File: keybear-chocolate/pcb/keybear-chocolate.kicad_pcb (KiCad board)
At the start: 2 copper layers, 136.9 x 98.2 mm, 102 parts, among them J1 MJ-4PP-9, J2 BATT, J3 LED, J4 OLED, SW1 SW_PUSH, SW10 SW_PUSH, SW11 SW_PUSH, SW12 SW_PUSH, SW13 SW_PUSH, SW14 SW_PUSH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

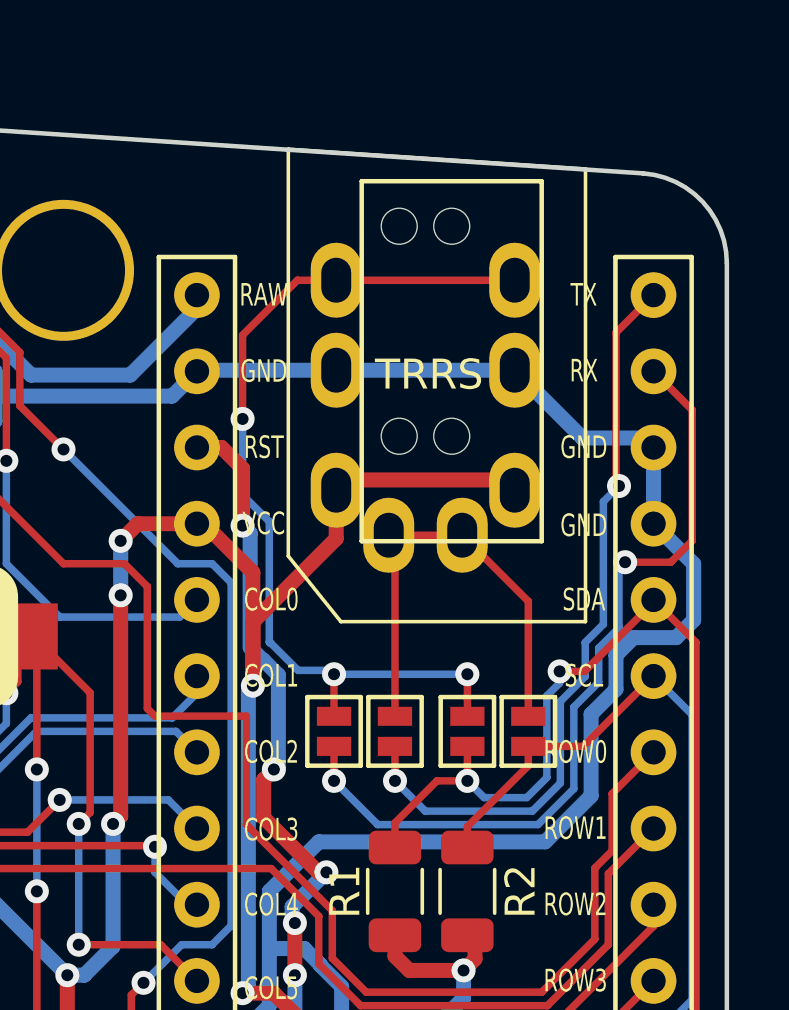
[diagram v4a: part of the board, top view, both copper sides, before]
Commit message: adding possible future pads
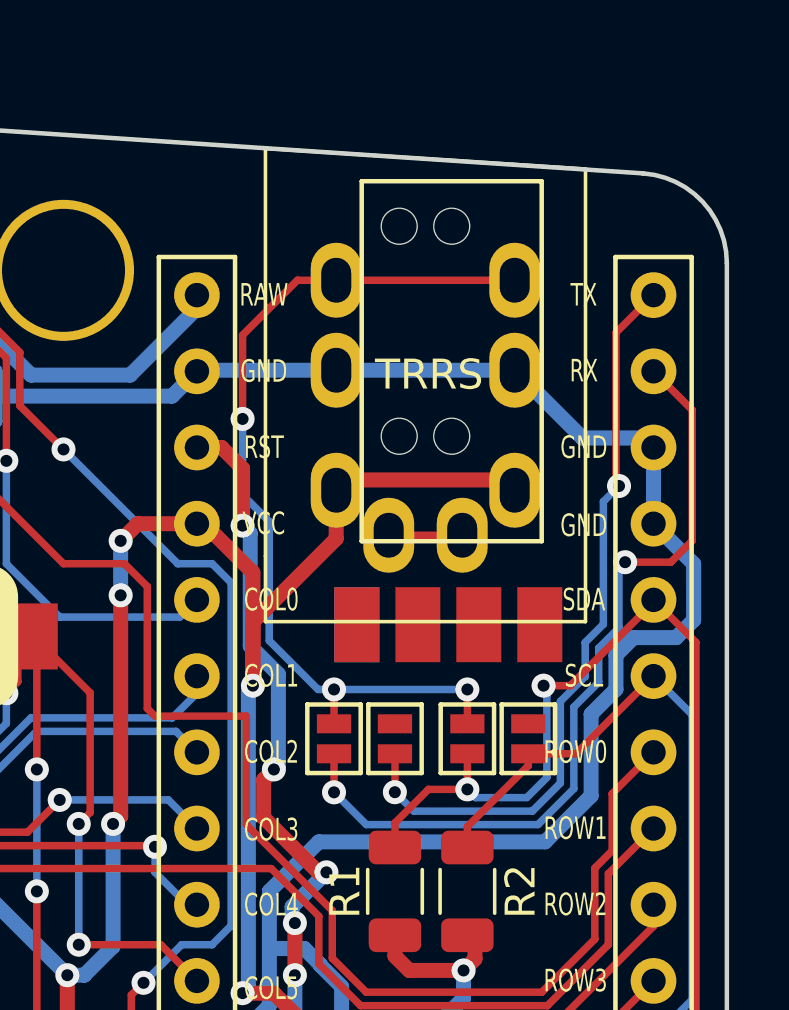
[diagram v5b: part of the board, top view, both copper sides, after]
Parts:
- added ?: , , F.Cu at (270.8, 111.0)
- added ?: , , F.Cu at (266.7, 111.0)
- added ?: , , F.Cu at (268.7, 111.0)
- added REF**: kb_hhole_d, kbd:kb_hhole_d, F.Cu at (264.7, 111.0)
- moved JP12 0.25 mm to (263.9, 114.8)
- moved JP13 0.25 mm to (265.9, 114.8)
- moved JP14 0.25 mm to (268.4, 114.8)
- moved JP15 0.25 mm to (270.4, 114.8)
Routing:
- net Net-(J1-PadA): track 15.5 -> 2.75 mm
- net Net-(J1-PadB): track 31.4 -> 30.5 mm

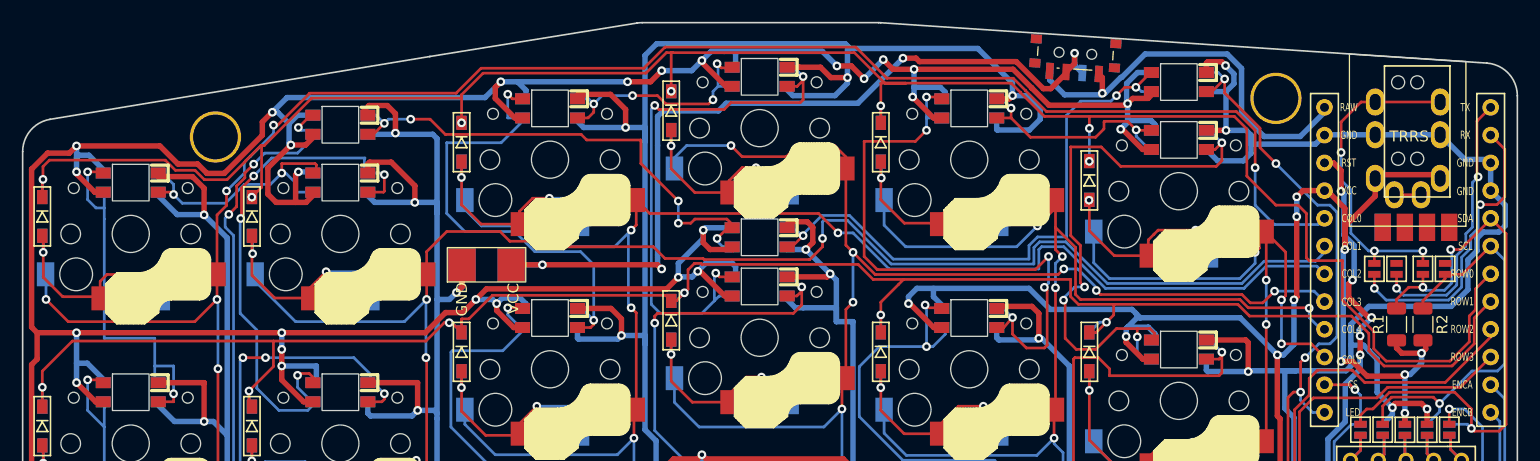
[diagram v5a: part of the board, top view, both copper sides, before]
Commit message: BEFORE USBC
I decided to do usbc instead of modular, just for now, to keep it simple...
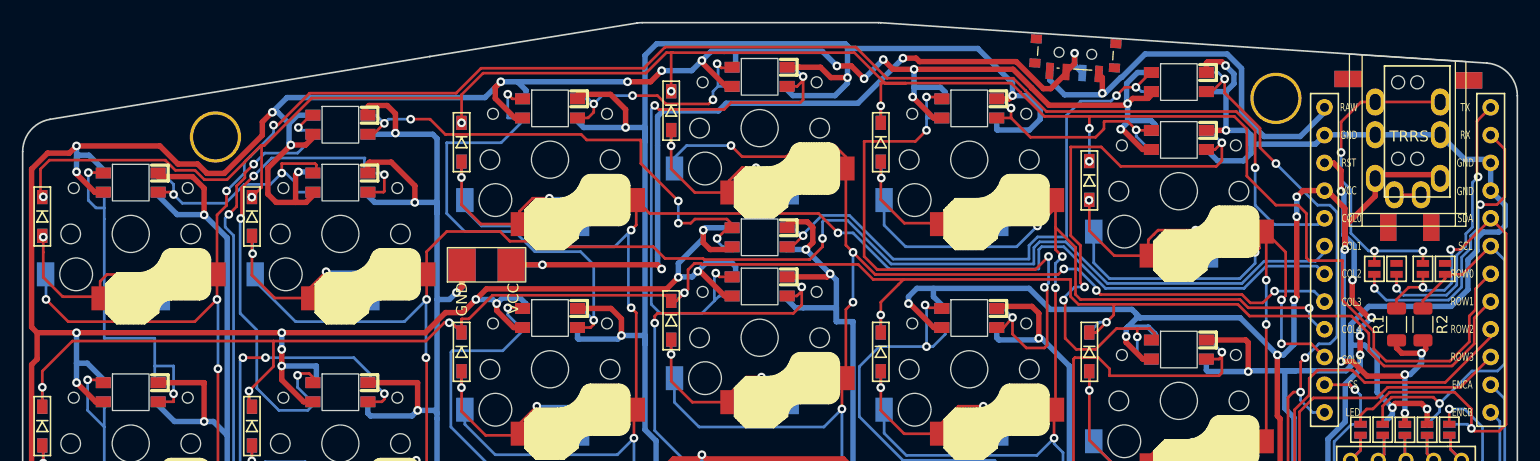
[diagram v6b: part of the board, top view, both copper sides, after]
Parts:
- removed ? (x3): , 
- added REF**: kb_hhole_d, kbd:kb_hhole_d, F.Cu at (265.2, 111.0)
- added REF**: kb_hhole_d, kbd:kb_hhole_d, F.Cu at (272.5, 97.5)
- added REF**: kb_hhole_d, kbd:kb_hhole_d, F.Cu at (269.1, 111.0)
- moved REF** 14.0 mm to (261.5, 97.4), turned to -90 degrees
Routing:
- net Net-(D1-A): track 20.8 -> 19.3 mm
- net row0: track 191.5 -> 190.1 mm

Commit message: usb-c added - WIP
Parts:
- removed REF** (x4): kb_hhole_d, kbd:kb_hhole_d
- added P1: USB_C_Plug, Connector_USB:USB_C_Receptacle_G-Switch_GT-USB-7010ASV, F.Cu at (266.9, 99.0)
- moved J1 36.2 mm to (299.4, 78.6)
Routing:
- net VCC: track 886.8 -> 891.6 mm
- net GND: track 905.9 -> 910.2 mm, vias 31 -> 33
- net Net-(J1-PadA): track 2.75 -> 0.00 mm
- net Net-(J1-PadB): track 30.5 -> 32.9 mm

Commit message: usb-c rx-tx connections added
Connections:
- J1 pad A: Net-(J1-PadA) -> Net-(P1-SBU1)
- JP13 pad 2: Net-(J1-PadA) -> Net-(P1-SBU1)
- JP15 pad 2: Net-(J1-PadA) -> Net-(P1-SBU1)
- P1 pad A6: unconnected-(P1-D+-PadA6) -> Net-(P1-SBU1)
- P1 pad A8: unconnected-(P1-SBU1-PadA8) -> Net-(P1-SBU1)
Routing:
- net Net-(P1-SBU1): track 0.00 -> 22.5 mm, vias 0 -> 2
